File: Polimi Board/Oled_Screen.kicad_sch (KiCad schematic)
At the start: 0 parts

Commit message: added programming oled and SD
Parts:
- added J5: Conn_01x04_Socket, symbol Connector:Conn_01x04_Socket
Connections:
- new net GND: J5.2 (Pin_2)
- new net Oled_SCL_I2C: J5.3 (Pin_3)
- new net Oled_SDA_I2C: J5.4 (Pin_4)
- new net VDD: J5.1 (Pin_1)
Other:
- company: (none) -> Politecnico di Milano
- title: (none) -> Polimi Board 
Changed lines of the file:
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@@
 (kicad_sch (version 20230121) (generator eeschema)
   (paper "A4")
+  (title_block
+    (title "Polimi Board ")
+    (date "2024-04-09")
+    (company "Politecnico di Milano")
+    (comment 1 "Embedded Systems")
+    (comment 2 "ing. Zaccaria Eliseo Carrettoni")
+  )
+  (wire (pts (xy 129.54 96.52) (xy 130.81 96.52))
+    (stroke (width 0) (type default))
+  )
+  (wire (pts (xy 127 93.98) (xy 127 99.06))
+    (stroke (width 0) (type default))
+  )
+  (wire (pts (xy 111.76 91.44) (xy 130.81 91.44))
+    (stroke (width 0) (type default))
+  )
+  (wire (pts (xy 107.95 101.6) (xy 129.54 101.6))
+    (stroke (width 0) (type default))
+  )
+  (wire (pts (xy 111.76 88.9) (xy 130.81 88.9))
+    (stroke (width 0) (type default))
+  )
+  (wire (pts (xy 107.95 99.06) (xy 127 99.06))
+    (stroke (width 0) (type default))
+  )
+  (wire (pts (xy 129.54 96.52) (xy 129.54 101.6))
+    (stroke (width 0) (type default))
+  )
+  (wire (pts (xy 127 93.98) (xy 130.81 93.98))
+    (stroke (width 0) (type default))
+  )
+  (hierarchical_label "Oled_SDA_I2C" (shape input) (at 107.95 101.6 180) (fields_autoplaced)
+    (effects (font (size 1.27 1.27)) (justify right))
+  )
+  (hierarchical_label "Oled_SCL_I2C" (shape input) (at 107.95 99.06 180) (fields_autoplaced)
+    (effects (font (size 1.27 1.27)) (justify right))
+  )
+  (symbol (lib_id "power:VDD") (at 111.76 88.9 0) (unit 1)
+    (in_bom yes) (on_board yes) (dnp no)
+    (property "Reference" "#PWR026" (at 111.76 92.71 0)
+      (effects (font (size 1.27 1.27)) hide)
+    )
+    (property "Value" "VDD" (at 111.76 85.09 0)
+      (effects (font (size 1.27 1.27)))
+    )
+    (property "Footprint" "" (at 111.76 88.9 0)
+      (effects (font (size 1.27 1.27)) hide)
+    )
+    (property "Datasheet" "" (at 111.76 88.9 0)
+      (effects (font (size 1.27 1.27)) hide)
+    )
+    (pin "1")
+    (instances
+      (project "Polimi Board"
+        (path "/319fe76e-1f98-44b3-99b0-af1a9ad7322c/108d9b54-87bf-4732-a1b8-edcdb25241bc"
+          (reference "#PWR026") (unit 1)
+        )
+      )
+    )
+  )
+  (symbol (lib_id "Connector:Conn_01x04_Socket") (at 135.89 91.44 0) (unit 1)
+    (in_bom yes) (on_board yes) (dnp no) (fields_autoplaced)
+    (property "Reference" "J5" (at 137.16 91.44 0)
+      (effects (font (size 1.27 1.27)) (justify left))
+    )
+    (property "Value" "Conn_01x04_Socket" (at 137.16 93.98 0)
+      (effects (font (size 1.27 1.27)) (justify left))
+    )
+    (property "Footprint" "" (at 135.89 91.44 0)
+      (effects (font (size 1.27 1.27)) hide)
+    )
+    (property "Datasheet" "~" (at 135.89 91.44 0)
+      (effects (font (size 1.27 1.27)) hide)
+    )
+    (pin "1")
+    (pin "2")
+    (pin "3")
+    (pin "4")
+    (instances
+      (project "Polimi Board"
+        (path "/319fe76e-1f98-44b3-99b0-af1a9ad7322c/108d9b54-87bf-4732-a1b8-edcdb25241bc"
+          (reference "J5") (unit 1)
+        )
+      )
+    )
+  )
+  (symbol (lib_id "power:GND") (at 111.76 91.44 0) (unit 1)
+    (in_bom yes) (on_board yes) (dnp no)
+    (property "Reference" "#PWR027" (at 111.76 97.79 0)
+      (effects (font (size 1.27 1.27)) hide)
+    )
+    (property "Value" "GND" (at 111.76 95.25 0)
+      (effects (font (size 1.27 1.27)))
+    )
+    (property "Footprint" "" (at 111.76 91.44 0)
+      (effects (font (size 1.27 1.27)) hide)
+    )
+    (property "Datasheet" "" (at 111.76 91.44 0)
+      (effects (font (size 1.27 1.27)) hide)
+    )
+    (pin "1")
+    (instances
+      (project "Polimi Board"
+        (path "/319fe76e-1f98-44b3-99b0-af1a9ad7322c/108d9b54-87bf-4732-a1b8-edcdb25241bc"
+          (reference "#PWR027") (unit 1)
+        )
+      )
+    )
+  )
 )

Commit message: Finish schematic part
To be reviewd
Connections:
- net GND renamed gnd
- net VDD renamed Vdd
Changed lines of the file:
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@@
   (title_block
     (title "Polimi Board ")
-    (date "2024-04-09")
+    (date "2024-04-24")
     (rev "1.0")
     (company "Politecnico di Milano")
-    (comment 1 "Embedded Systems")
+    (comment 1 "Embedded Systems Project")
     (comment 2 "ing. Zaccaria Eliseo Carrettoni")
   )
-  (wire (pts (xy 129.54 96.52) (xy 130.81 96.52))
+  (wire (pts (xy 120.65 96.52) (xy 130.81 96.52))
     (stroke (width 0) (type default))
   )
-  (wire (pts (xy 127 93.98) (xy 127 99.06))
+  (wire (pts (xy 120.65 91.44) (xy 130.81 91.44))
     (stroke (width 0) (type default))
   )
-  (wire (pts (xy 111.76 91.44) (xy 130.81 91.44))
+  (wire (pts (xy 120.65 88.9) (xy 130.81 88.9))
     (stroke (width 0) (type default))
   )
-  (wire (pts (xy 107.95 101.6) (xy 129.54 101.6))
+  (wire (pts (xy 120.65 93.98) (xy 130.81 93.98))
     (stroke (width 0) (type default))
   )
-  (wire (pts (xy 111.76 88.9) (xy 130.81 88.9))
-    (stroke (width 0) (type default))
-  )
-  (wire (pts (xy 107.95 99.06) (xy 127 99.06))
-    (stroke (width 0) (type default))
-  )
-  (wire (pts (xy 129.54 96.52) (xy 129.54 101.6))
-    (stroke (width 0) (type default))
-  )
-  (wire (pts (xy 127 93.98) (xy 130.81 93.98))
-    (stroke (width 0) (type default))
-  )
-  (hierarchical_label "Oled_SDA_I2C" (shape input) (at 107.95 101.6 180) (fields_autoplaced)
+  (hierarchical_label "Oled_SDA_I2C" (shape input) (at 120.65 96.52 180) (fields_autoplaced)
     (effects (font (size 1.27 1.27)) (justify right))
   )
-  (hierarchical_label "Oled_SCL_I2C" (shape input) (at 107.95 99.06 180) (fields_autoplaced)
+  (hierarchical_label "Oled_SCL_I2C" (shape input) (at 120.65 93.98 180) (fields_autoplaced)
     (effects (font (size 1.27 1.27)) (justify right))
   )
-  (symbol (lib_id "power:VDD") (at 111.76 88.9 0) (unit 1)
-    (in_bom yes) (on_board yes) (dnp no)
-    (property "Reference" "#PWR026" (at 111.76 92.71 0)
-      (effects (font (size 1.27 1.27)) hide)
-    )
-    (property "Value" "VDD" (at 111.76 85.09 0)
-      (effects (font (size 1.27 1.27)))
-    )
-    (property "Footprint" "" (at 111.76 88.9 0)
-      (effects (font (size 1.27 1.27)) hide)
-    )
-    (property "Datasheet" "" (at 111.76 88.9 0)
-      (effects (font (size 1.27 1.27)) hide)
-    )
-    (pin "1")
-    (instances
-      (project "Polimi Board"
-        (path "/319fe76e-1f98-44b3-99b0-af1a9ad7322c/108d9b54-87bf-4732-a1b8-edcdb25241bc"
-          (reference "#PWR026") (unit 1)
-        )
-      )
-    )
+  (hierarchical_label "gnd" (shape input) (at 120.65 91.44 180) (fields_autoplaced)
+    (effects (font (size 1.27 1.27)) (justify right))
+  )
+  (hierarchical_label "Vdd" (shape input) (at 120.65 88.9 180) (fields_autoplaced)
+    (effects (font (size 1.27 1.27)) (justify right))
   )
   (symbol (lib_id "Connector:Conn_01x04_Socket") (at 135.89 91.44 0) (unit 1)
@@
         )
       )
-    )
-  )
-  (symbol (lib_id "power:GND") (at 111.76 91.44 0) (unit 1)
-    (in_bom yes) (on_board yes) (dnp no)
-    (property "Reference" "#PWR027" (at 111.76 97.79 0)
-      (effects (font (size 1.27 1.27)) hide)
-    )
-    (property "Value" "GND" (at 111.76 95.25 0)
-      (effects (font (size 1.27 1.27)))
-    )
-    (property "Footprint" "" (at 111.76 91.44 0)
-      (effects (font (size 1.27 1.27)) hide)
-    )
-    (property "Datasheet" "" (at 111.76 91.44 0)
-      (effects (font (size 1.27 1.27)) hide)
-    )
-    (pin "1")
-    (instances
-      (project "Polimi Board"
-        (path "/319fe76e-1f98-44b3-99b0-af1a9ad7322c/108d9b54-87bf-4732-a1b8-edcdb25241bc"
-          (reference "#PWR027") (unit 1)
-        )
-      )

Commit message: Fatte modifiche
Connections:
- net Vdd renamed GND
- net gnd renamed +3.3V
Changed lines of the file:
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@@
   (title_block
     (title "Polimi Board ")
-    (date "2024-04-24")
-    (rev "1.0")
+    (date "2024-04-29")
+    (rev "2.0")
     (company "Politecnico di Milano")
     (comment 1 "Embedded Systems Project")
@@
     (stroke (width 0) (type default))
   )
-  (wire (pts (xy 120.65 91.44) (xy 130.81 91.44))
+  (wire (pts (xy 121.92 85.09) (xy 121.92 91.44))
     (stroke (width 0) (type default))
   )
-  (wire (pts (xy 120.65 88.9) (xy 130.81 88.9))
+  (wire (pts (xy 128.27 88.9) (xy 128.27 85.09))
+    (stroke (width 0) (type default))
+  )
+  (wire (pts (xy 128.27 88.9) (xy 130.81 88.9))
+    (stroke (width 0) (type default))
+  )
+  (wire (pts (xy 121.92 91.44) (xy 130.81 91.44))
     (stroke (width 0) (type default))
   )
@@
     (effects (font (size 1.27 1.27)) (justify right))
   )
-  (hierarchical_label "gnd" (shape input) (at 120.65 91.44 180) (fields_autoplaced)
-    (effects (font (size 1.27 1.27)) (justify right))
-  )
-  (hierarchical_label "Vdd" (shape input) (at 120.65 88.9 180) (fields_autoplaced)
-    (effects (font (size 1.27 1.27)) (justify right))
+  (symbol (lib_id "power:+3.3V") (at 121.92 85.09 0) (unit 1)
+    (in_bom yes) (on_board yes) (dnp no) (fields_autoplaced)
+    (property "Reference" "#PWR030" (at 121.92 88.9 0)
+      (effects (font (size 1.27 1.27)) hide)
+    )
+    (property "Value" "+3.3V" (at 121.92 80.01 0)
+      (effects (font (size 1.27 1.27)))
+    )
+    (property "Footprint" "" (at 121.92 85.09 0)
+      (effects (font (size 1.27 1.27)) hide)
+    )
+    (property "Datasheet" "" (at 121.92 85.09 0)
+      (effects (font (size 1.27 1.27)) hide)
+    )
+    (pin "1")
+    (instances
+      (project "Polimi Board"
+        (path "/319fe76e-1f98-44b3-99b0-af1a9ad7322c/108d9b54-87bf-4732-a1b8-edcdb25241bc"
+          (reference "#PWR030") (unit 1)
+        )
+      )
+    )
   )
   (symbol (lib_id "Connector:Conn_01x04_Socket") (at 135.89 91.44 0) (unit 1)
@@
         )
       )
+    )
+  )
+  (symbol (lib_id "power:GND") (at 128.27 85.09 180) (unit 1)
+    (in_bom yes) (on_board yes) (dnp no) (fields_autoplaced)
+    (property "Reference" "#PWR026" (at 128.27 78.74 0)
+      (effects (font (size 1.27 1.27)) hide)
+    )
+    (property "Value" "GND" (at 128.27 80.01 0)
+      (effects (font (size 1.27 1.27)))
+    )
+    (property "Footprint" "" (at 128.27 85.09 0)
+      (effects (font (size 1.27 1.27)) hide)
+    )
+    (property "Datasheet" "" (at 128.27 85.09 0)
+      (effects (font (size 1.27 1.27)) hide)
+    )
+    (pin "1")
+    (instances
+      (project "Polimi Board"
+        (path "/319fe76e-1f98-44b3-99b0-af1a9ad7322c/108d9b54-87bf-4732-a1b8-edcdb25241bc"
+          (reference "#PWR026") (unit 1)
+        )
+      )

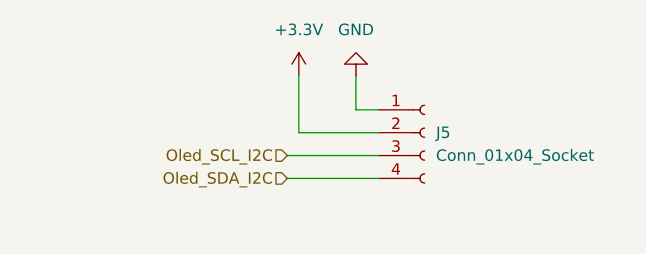
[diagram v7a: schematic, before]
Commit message: Added footprint from Mouser
readu for wiring
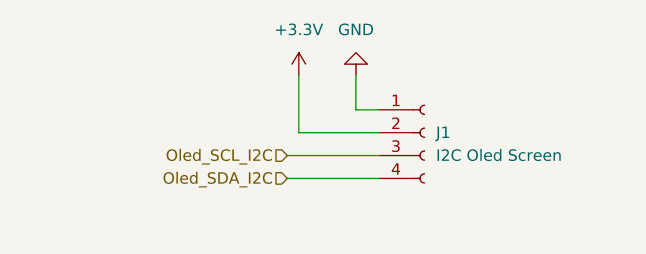
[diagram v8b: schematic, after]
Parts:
- J1: renamed from J5; value Conn_01x04_Socket -> I2C Oled Screen; footprint (none) -> Connector_PinSocket_2.54mm:PinSocket_1x04_P2.54mm_Vertical
